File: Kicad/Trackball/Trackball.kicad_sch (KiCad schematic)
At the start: 66 parts, among them J1 Battery, J10 Conn_01x04_Female, J11 Conn_01x04_Female, J12 Conn_01x04_Female, J13 Conn_01x04_Female, J14 Conn_01x04_Female, J15 Conn_01x04_Female, J17 Conn_01x04_Female, J18 Conn_01x03_Pin, J19 Conn_01x03_Pin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

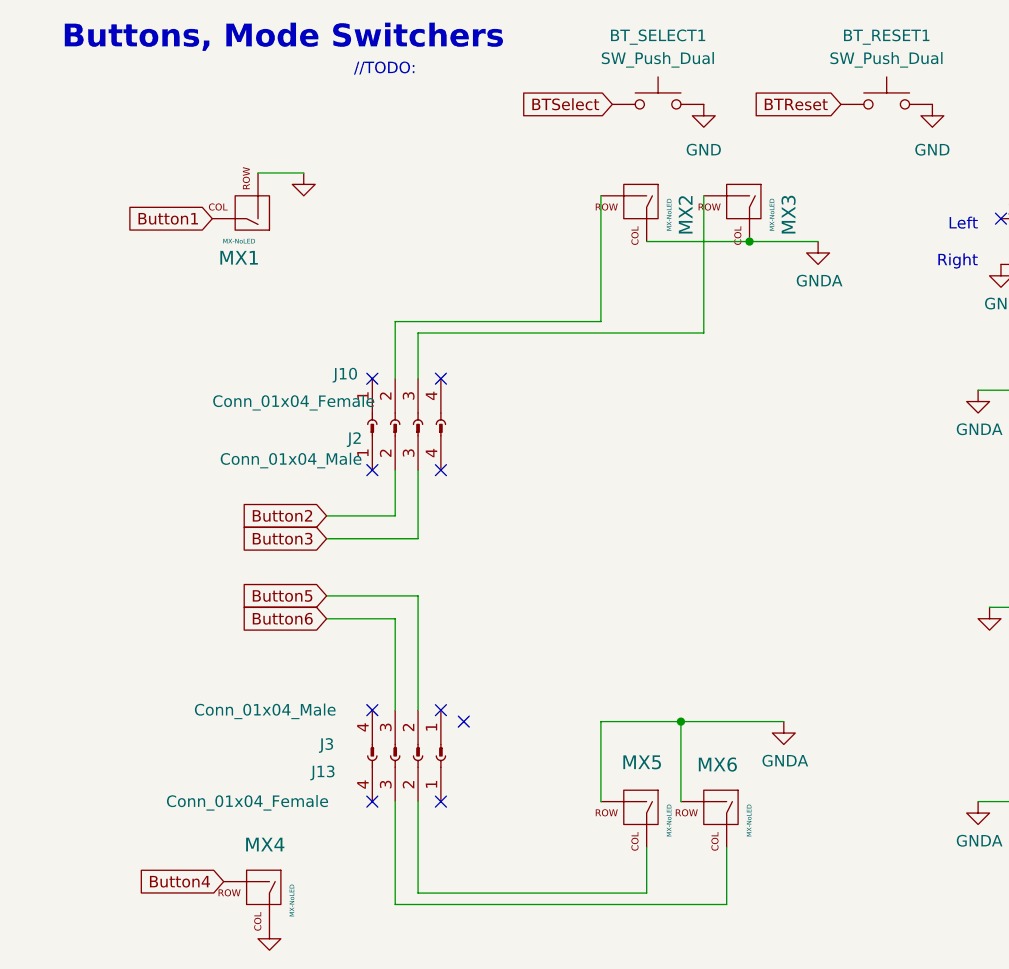
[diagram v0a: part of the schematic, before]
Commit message: B5: Replaced switches, added soldering pad switches to configure the button switch orientation, added break-outs to detach the flaps over the switches.
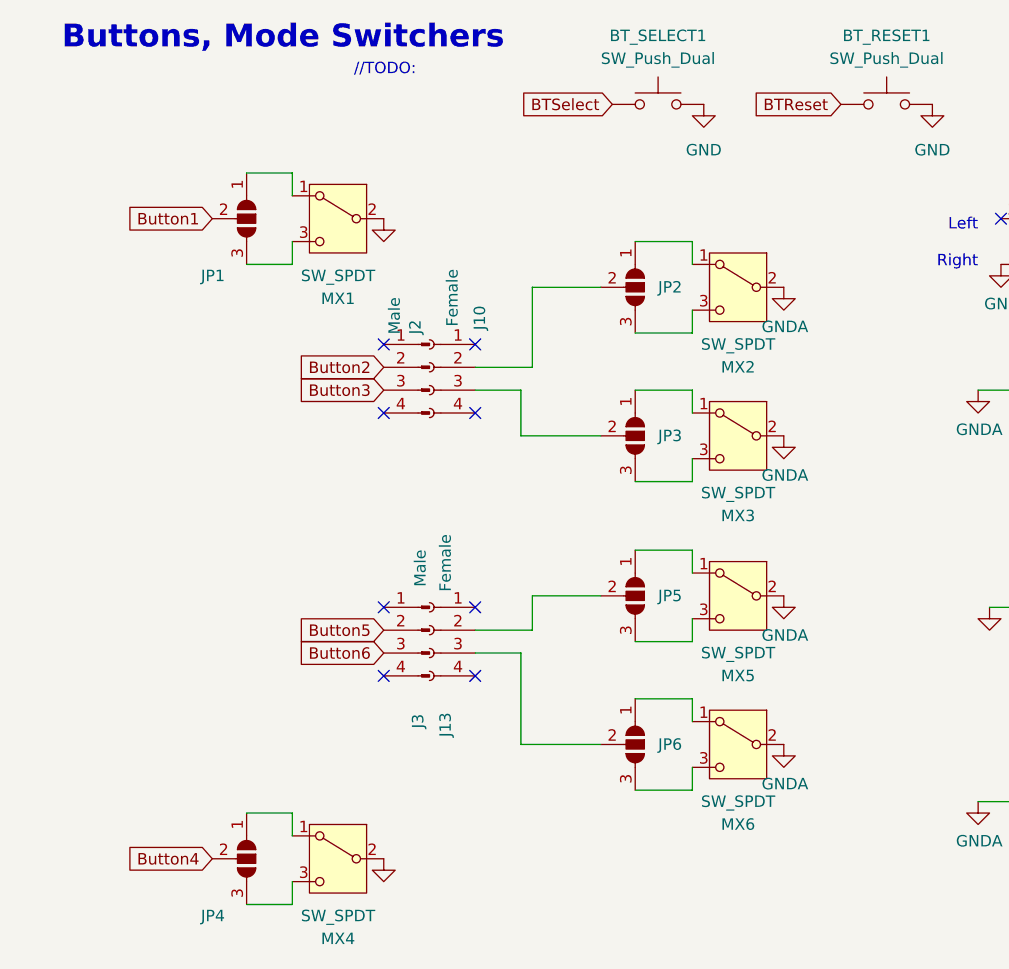
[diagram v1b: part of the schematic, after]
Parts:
- removed MX1, MX2, MX3, MX4, MX5, MX6: MX-NoLED, footprints:SW_D2FC_OMR, symbol MX_Alps_Hybrid:MX-NoLED
- added JP1, JP2, JP3, JP4, JP5, JP6: SolderJumper_3_Open, Jumper:SolderJumper-3_P1.3mm_Open_RoundedPad1.0x1.5mm, symbol Jumper:SolderJumper_3_Open
- added MX1, MX2, MX3, MX4, MX5, MX6: SW_SPDT, footprints:SW_D2FC_OMR, symbol Switch:SW_SPDT
- J10, J13: value Conn_01x04_Female -> Female
- J2, J3: value Conn_01x04_Male -> Male
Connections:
- net Button1: now also JP1.2 (C)
- net Button4: now also JP4.2 (C)
- net GND: now also MX1.2 (B), MX4.2 (B)
- net GNDA: now also MX2.2 (B), MX3.2 (B), MX5.2 (B), MX6.2 (B)
- net at J10.2 (Pin_2): now also JP2.2 (C)
- net at J10.3 (Pin_3): now also JP3.2 (C)
- net at J13.2 (Pin_2): now also JP5.2 (C)
- net at J13.3 (Pin_3): now also JP6.2 (C)
- new net: JP1.1 (A), MX1.1 (A)
- new net: JP1.3 (B), MX1.3 (C)
- new net: JP5.1 (A), MX5.1 (A)
- new net: JP5.3 (B), MX5.3 (C)
- new net: JP2.1 (A), MX2.1 (A)
- new net: JP2.3 (B), MX2.3 (C)
- new net: JP4.1 (A), MX4.1 (A)
- new net: JP4.3 (B), MX4.3 (C)
- new net: JP3.1 (A), MX3.1 (A)
- new net: JP3.3 (B), MX3.3 (C)
- new net: JP6.1 (A), MX6.1 (A)
- new net: JP6.3 (B), MX6.3 (C)
- no-connect marks 11 -> 10
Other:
- moved on the sheet: J10, J13, J2, J3

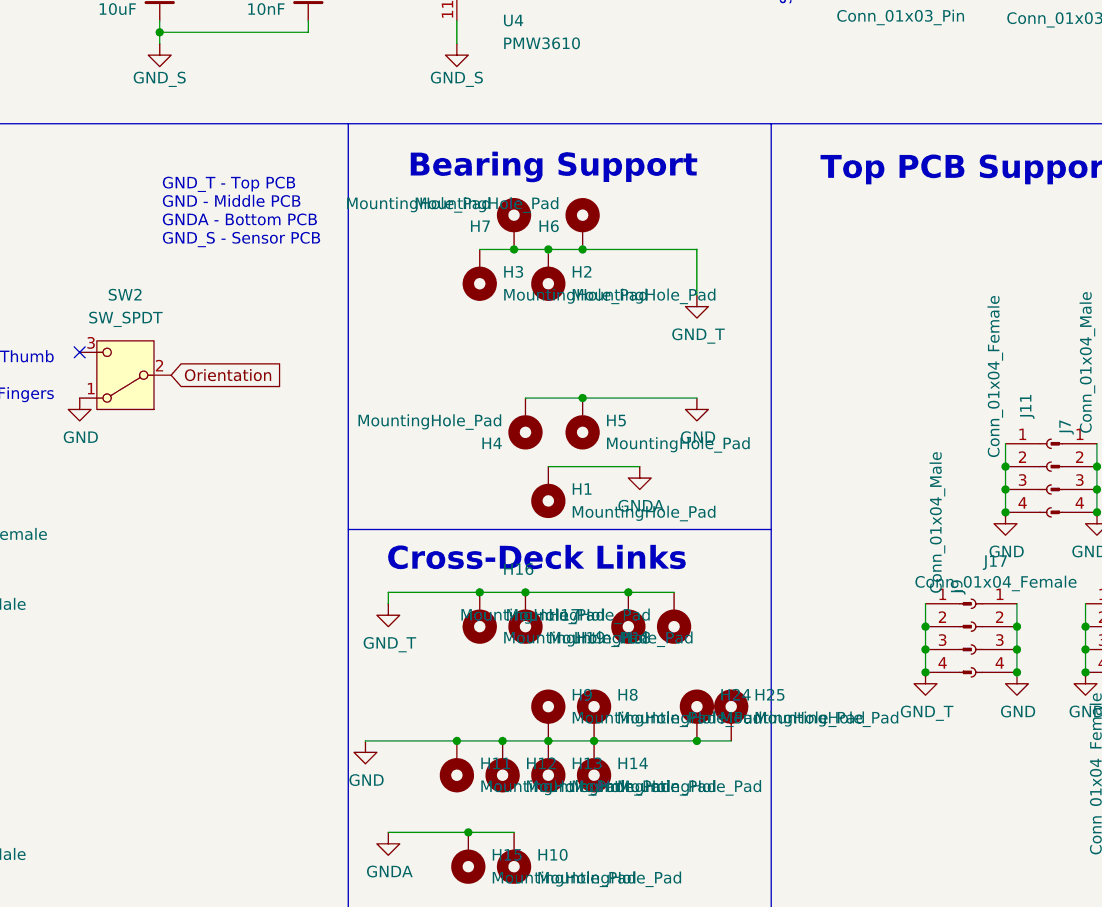
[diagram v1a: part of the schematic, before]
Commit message: B5: Separated key flaps into a separate panel. Added photos of rev.1 device.
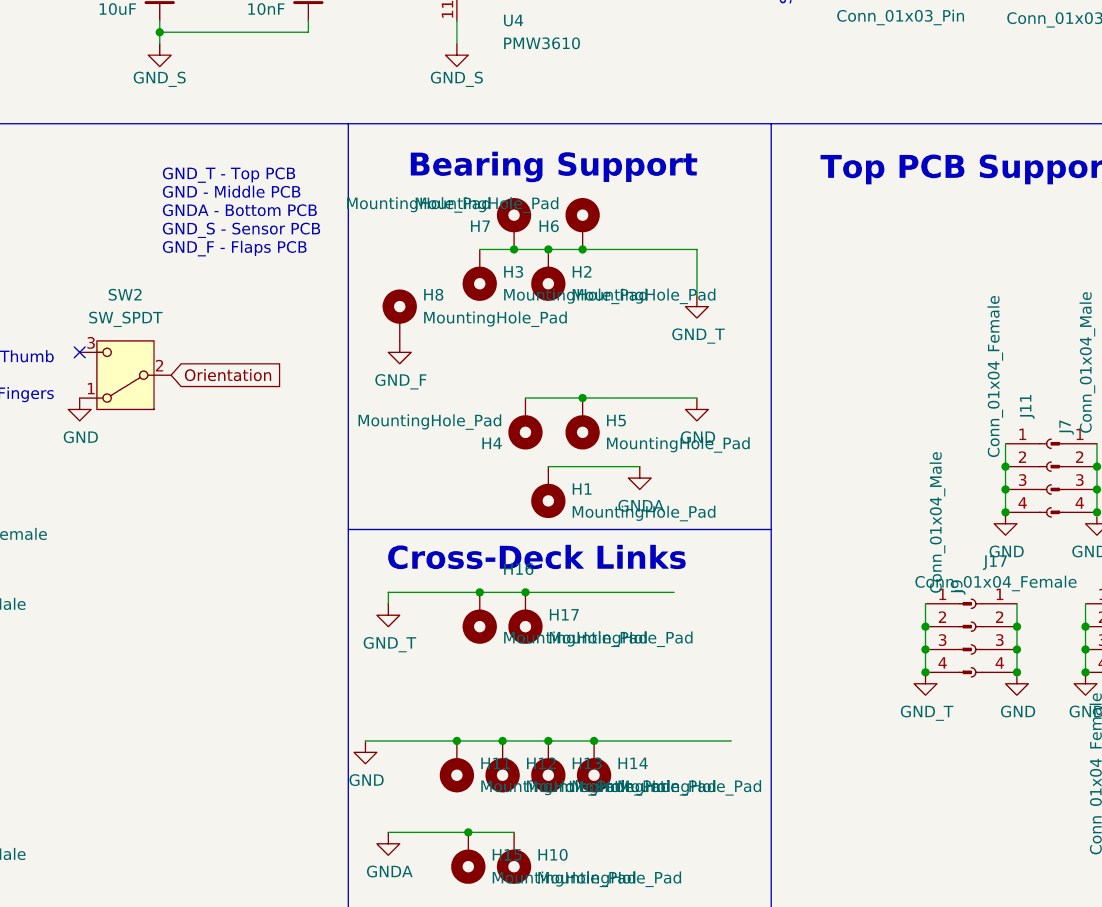
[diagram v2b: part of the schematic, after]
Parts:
- removed H18, H19, H24, H25, H9: MountingHole_Pad, ButtonLevers:ButtonLever_HingeSlot, symbol Mechanical:MountingHole_Pad
- H8: footprint ButtonLevers:ButtonLever_HingeSlot -> MountingHole:MountingHole_2.5mm_Pad
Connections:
- net GND: no longer H8.1
- new net GND_F: H8.1
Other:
- note added: "GND_T - Top PCB GND - Middle PCB GNDA - Bottom PCB GND_S - Sensor PCB GND_F - Flaps PCB"
- note removed: "GND_T - Top PCB GND - Middle PCB GNDA - Bottom PCB GND_S - Sensor PCB"

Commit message: B5: Rev.1 changes.
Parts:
- removed H2, H3: MountingHole_Pad, MountingHole:MountingHole_2.5mm_Pad, symbol Mechanical:MountingHole_Pad
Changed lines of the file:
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@@
 	)
 	(junction
-		(at 208.28 91.44)
-		(diameter 0)
-		(color 0 0 0 0)
-	)
-	(junction
 		(at 267.97 138.43)
 		(diameter 0)
@@
 	(wire
 		(pts
-			(xy 204.47 91.44) (xy 208.28 91.44)
-		)
-		(stroke
-			(width 0)
-			(type default)
-		)
-	)
-	(wire
-		(pts
 			(xy 87.63 149.86) (xy 87.63 147.32)
 		)
@@
 	(wire
 		(pts
-			(xy 208.28 91.44) (xy 212.09 91.44)
+			(xy 204.47 91.44) (xy 212.09 91.44)
 		)
 		(stroke
@@
 	)
 	(symbol
-		(lib_id "Mechanical:MountingHole_Pad")
-		(at 208.28 93.98 180)
-		(unit 1)
-		(exclude_from_sim no)
-		(in_bom no)
-		(on_board yes)
-		(dnp no)
-		(fields_autoplaced yes)
-		(property "Reference" "H2"
-			(at 210.82 93.9799 0)
-			(effects
-				(font
-					(size 1.27 1.27)
-				)
-				(justify right)
-			)
-		)
-		(property "Value" "MountingHole_Pad"
-			(at 210.82 96.5199 0)
-			(effects
-				(font
-					(size 1.27 1.27)
-				)
-				(justify right)
-			)
-		)
-		(property "Footprint" "MountingHole:MountingHole_2.5mm_Pad"
-			(at 208.28 93.98 0)
-			(effects
-				(font
-					(size 1.27 1.27)
-				)
-				(hide yes)
-			)
-		)
-		(property "Datasheet" "~"
-			(at 208.28 93.98 0)
-			(effects
-				(font
-					(size 1.27 1.27)
-				)
-				(hide yes)
-			)
-		)
-		(property "Description" "Mounting Hole with connection"
-			(at 208.28 93.98 0)
-			(effects
-				(font
-					(size 1.27 1.27)
-				)
-				(hide yes)
-			)
-		)
-		(pin "1"
-		)
-		(instances
-			(project "Trackball"
-				(path "/8cc78baa-4975-41f7-8a0a-10f41c28d40d"
-					(reference "H2")
-					(unit 1)
-				)
-			)
-		)
-	)
-	(symbol
 		(lib_id "Device:C_Small")
 		(at 165.1 63.5 0)
@@
 					(unit 1)
 				)
-			)
-		)
-	)
-	(symbol
-		(lib_id "Mechanical:MountingHole_Pad")
-		(at 200.66 93.98 180)
-		(unit 1)
-		(exclude_from_sim no)
-		(in_bom no)
-		(on_board yes)
-		(dnp no)
-		(fields_autoplaced yes)
-		(property "Reference" "H3"
-			(at 203.2 93.9799 0)
-			(effects
-				(font
-					(size 1.27 1.27)
-				)
-				(justify right)
-			)
-		)
-		(property "Value" "MountingHole_Pad"
-			(at 203.2 96.5199 0)
-			(effects
-				(font
-					(size 1.27 1.27)
-				)
-				(justify right)
-			)
-		)
-		(property "Footprint" "MountingHole:MountingHole_2.5mm_Pad"
-			(at 200.66 93.98 0)
-			(effects
-				(font
-					(size 1.27 1.27)
-				)
-				(hide yes)
-			)
-		)
-		(property "Datasheet" "~"
-			(at 200.66 93.98 0)
-			(effects
-				(font
-					(size 1.27 1.27)
-				)
-				(hide yes)
-			)
-		)
-		(property "Description" "Mounting Hole with connection"
-			(at 200.66 93.98 0)
-			(effects
-				(font
-					(size 1.27 1.27)
-				)
-				(hide yes)
-			)
-		)
-		(pin "1"
-		)
-		(instances
-			(project "Trackball"
-				(path "/8cc78baa-4975-41f7-8a0a-10f41c28d40d"
-					(reference "H3")
-					(unit 1)
-				)
